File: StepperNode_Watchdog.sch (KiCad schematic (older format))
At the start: 5 parts

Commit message: First Revision -
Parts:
- removed R? (x2): 10K, symbol R
- removed U? (x2): TPS3813, symbol TPS3813
- removed U?: 74LVC1G32GW,125, symbol 74LVC1G32GW,125
- added R10, R9: 10K, RLOOP_FOOTPRINTS:rLoop_R_0603, symbol 10K
- added R5, R6, R7, R8: 0R, RLOOP_FOOTPRINTS:rLoop_R_0603, symbol 0R
- added U10, U11: TPS3813K33DBVT, RLOOP_FOOTPRINTS:rLoop_SOT236, symbol TPS3813K33DBVT
- added U12: 74LVC1G32GW,125, RLOOP_FOOTPRINTS:rLoop_SOT353, symbol 74LVC1G32GW,125
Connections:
- net labels added: +3V3_A, +3V3_B, GNDD
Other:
- note added: "DESIGN REVIEW NOTES:\n1. STEP_DIR_CTRL should go low if channel A fails, giving channel B priority\n2. STEP_DIR_CTRL is pulled up, so the only way it can go low is if the TPS3813 is powered\n3. All devices here need redundant supplies\n4. Need to provide isolation in case of parasitic power from a failed node."

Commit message: Update per design review.
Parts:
- added C? (x3): C_100nF_50V, RLOOP_FOOTPRINTS:rLoop_C_0603, symbol C_100nF_50V
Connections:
- net +3V3: now also C?.1, C?.1, C?.1
- net GNDD: now also C?.2, C?.2, C?.2
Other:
- note added: "Active High when either watchdog is good.\nThis signal then ensure the G210X enable circuits are kept closed except in\nthe case of a dual channel failure, where failsafe braking is required."
- note removed: "Active High when\nBoth watchdogs are good"
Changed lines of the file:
@@
 Title "Watchdog"
 Date ""
-Rev "1"
+Rev "2"
 Comp ""
 Comment1 ""
@@
 Text Label 9850 5150 0    60   ~ 0
 WDT_GOOD
-Text Notes 10000 5400 0    60   ~ 0
-Active High when\nBoth watchdogs are good
+Text Notes 10000 5600 0    60   ~ 0
+Active High when either watchdog is good.\nThis signal then ensure the G210X enable circuits are kept closed except in\nthe case of a dual channel failure, where failsafe braking is required.
 Text Notes 5750 6600 0    60   ~ 0
 Todo:\nJumper Pin to simulate failures.
@@
 	0    -1   -1   0
 $EndComp
+$Comp
+L C_100nF_50V C?
+U 1 1 575CF20D
+P 4150 4950
+F 0 "C?" H 4175 5050 50  0000 L CNN
+F 1 "C_100nF_50V" H 4175 4850 50  0000 L CNN
+F 2 "RLOOP_FOOTPRINTS:rLoop_C_0603" H 4188 4800 50  0001 C CNN
+F 3 "" H 4150 4950 50  0000 C CNN
+	1    4150 4950
+	1    0    0    -1
+$EndComp
+$Comp
+L +3V3_A #PWR?
+U 1 1 575CF256
+P 4150 4800
+F 0 "#PWR?" H 4150 4650 50  0001 C CNN
+F 1 "+3V3_A" H 4150 4940 50  0000 C CNN
+F 2 "" H 4150 4800 60  0000 C CNN
+F 3 "" H 4150 4800 60  0000 C CNN
+	1    4150 4800
+	1    0    0    -1
+$EndComp
+$Comp
+L GNDD #PWR?
+U 1 1 575CF268
+P 4150 5100
+F 0 "#PWR?" H 4150 4850 50  0001 C CNN
+F 1 "GNDD" H 4150 4950 50  0000 C CNN
+F 2 "" H 4150 5100 50  0000 C CNN
+F 3 "" H 4150 5100 50  0000 C CNN
+	1    4150 5100
+	1    0    0    -1
+$EndComp
+$Comp
+L C_100nF_50V C?
+U 1 1 575CF2F4
+P 4150 6050
+F 0 "C?" H 4175 6150 50  0000 L CNN
+F 1 "C_100nF_50V" H 4175 5950 50  0000 L CNN
+F 2 "RLOOP_FOOTPRINTS:rLoop_C_0603" H 4188 5900 50  0001 C CNN
+F 3 "" H 4150 6050 50  0000 C CNN
+	1    4150 6050
+	1    0    0    -1
+$EndComp
+$Comp
+L GNDD #PWR?
+U 1 1 575CF2FA
+P 4150 6200
+F 0 "#PWR?" H 4150 5950 50  0001 C CNN
+F 1 "GNDD" H 4150 6050 50  0000 C CNN
+F 2 "" H 4150 6200 50  0000 C CNN
+F 3 "" H 4150 6200 50  0000 C CNN
+	1    4150 6200
+	1    0    0    -1
+$EndComp
+$Comp
+L +3V3_B #PWR?
+U 1 1 575CF30D
+P 4150 5900
+F 0 "#PWR?" H 4150 5750 50  0001 C CNN
+F 1 "+3V3_B" H 4150 6040 50  0000 C CNN
+F 2 "" H 4150 5900 60  0000 C CNN
+F 3 "" H 4150 5900 60  0000 C CNN
+	1    4150 5900
+	1    0    0    -1
+$EndComp
+$Comp
+L C_100nF_50V C?
+U 1 1 575CF5E2
+P 9500 6200
+F 0 "C?" H 9525 6300 50  0000 L CNN
+F 1 "C_100nF_50V" H 9525 6100 50  0000 L CNN
+F 2 "RLOOP_FOOTPRINTS:rLoop_C_0603" H 9538 6050 50  0001 C CNN
+F 3 "" H 9500 6200 50  0000 C CNN
+	1    9500 6200
+	1    0    0    -1
+$EndComp
+$Comp
+L +3V3_A #PWR?
+U 1 1 575CF5E8
+P 9500 6050
+F 0 "#PWR?" H 9500 5900 50  0001 C CNN
+F 1 "+3V3_A" H 9500 6190 50  0000 C CNN
+F 2 "" H 9500 6050 60  0000 C CNN
+F 3 "" H 9500 6050 60  0000 C CNN
+	1    9500 6050
+	1    0    0    -1
+$EndComp
+$Comp
+L GNDD #PWR?
+U 1 1 575CF5EE
+P 9500 6350
+F 0 "#PWR?" H 9500 6100 50  0001 C CNN
+F 1 "GNDD" H 9500 6200 50  0000 C CNN
+F 2 "" H 9500 6350 50  0000 C CNN
+F 3 "" H 9500 6350 50  0000 C CNN
+	1    9500 6350
+	1    0    0    -1
+$EndComp
 $EndSCHEMATC

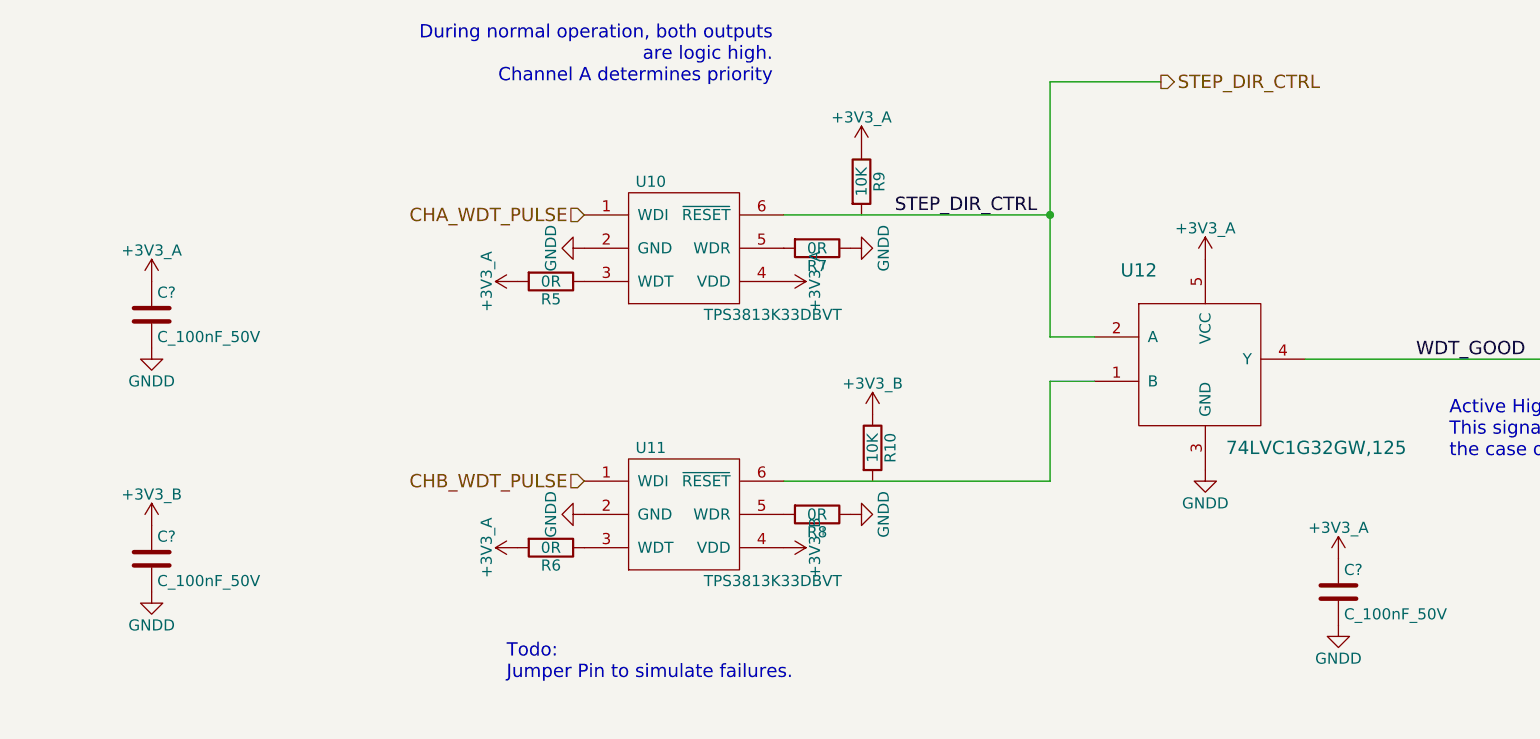
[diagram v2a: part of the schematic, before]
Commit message: Fix most ERC warnings (non-connected pins, etc)
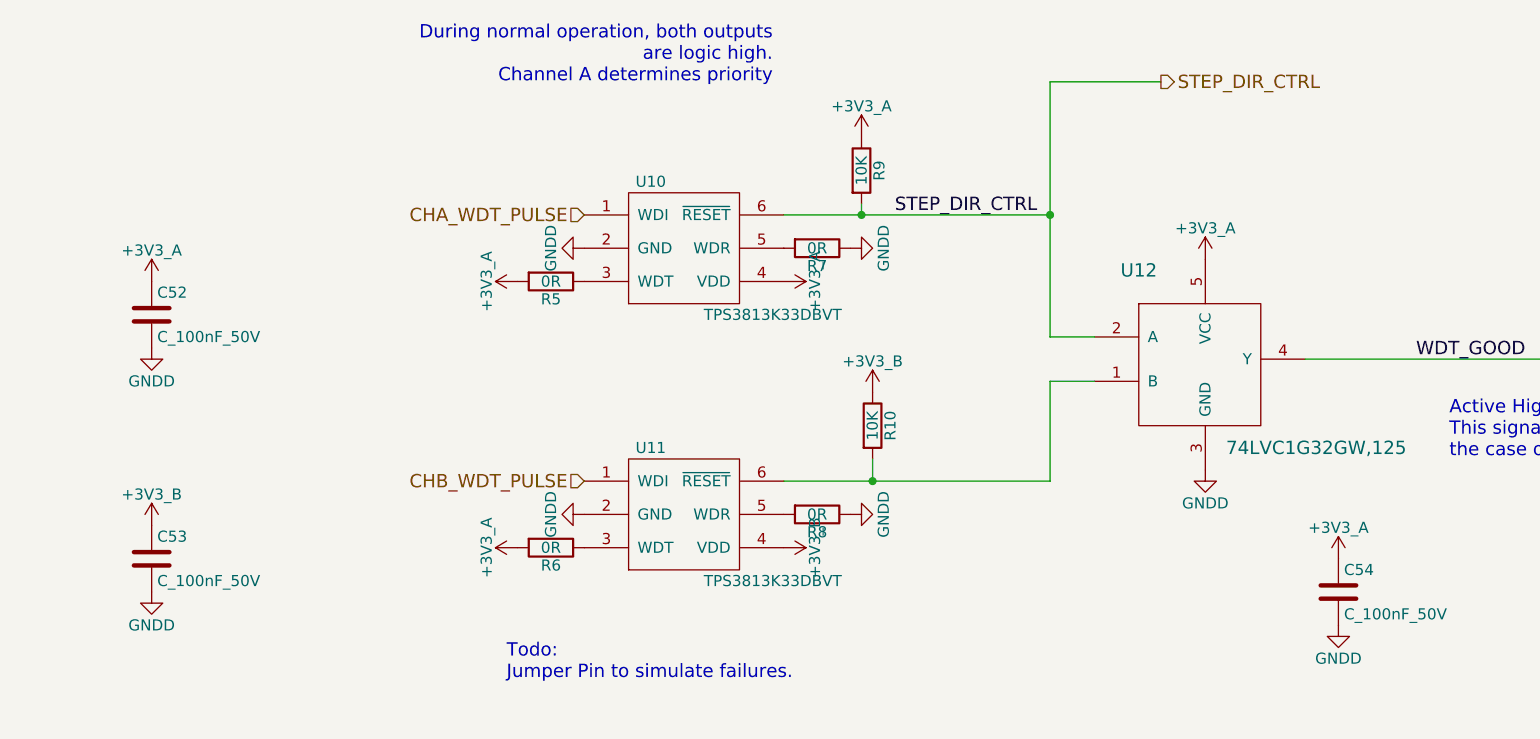
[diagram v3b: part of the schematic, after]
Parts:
- gave numbers to parts that had none: 3
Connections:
- net STEP_DIR_CTRL: now also R9.2
- net at R10.2: now also U11.6 (~RESET), U12.1 (B)
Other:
- moved on the sheet: R10, R9
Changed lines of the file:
@@
 L 10K R10
 U 1 1 575D4934
-P 7400 5550
-F 0 "R10" V 7480 5550 50  0000 C CNN
-F 1 "10K" V 7400 5550 50  0000 C CNN
-F 2 "RLOOP_FOOTPRINTS:rLoop_R_0603" V 7330 5550 50  0001 C CNN
-F 3 "" H 7400 5550 50  0000 C CNN
-	1    7400 5550
+P 7400 5450
+F 0 "R10" V 7480 5450 50  0000 C CNN
+F 1 "10K" V 7400 5450 50  0000 C CNN
+F 2 "RLOOP_FOOTPRINTS:rLoop_R_0603" V 7330 5450 50  0001 C CNN
+F 3 "" H 7400 5450 50  0000 C CNN
+	1    7400 5450
 	1    0    0    -1
 $EndComp
@@
 L 10K R9
 U 1 1 575D49D5
-P 7350 4350
-F 0 "R9" V 7430 4350 50  0000 C CNN
-F 1 "10K" V 7350 4350 50  0000 C CNN
-F 2 "RLOOP_FOOTPRINTS:rLoop_R_0603" V 7280 4350 50  0001 C CNN
-F 3 "" H 7350 4350 50  0000 C CNN
-	1    7350 4350
+P 7350 4300
+F 0 "R9" V 7430 4300 50  0000 C CNN
+F 1 "10K" V 7350 4300 50  0000 C CNN
+F 2 "RLOOP_FOOTPRINTS:rLoop_R_0603" V 7280 4300 50  0001 C CNN
+F 3 "" H 7350 4300 50  0000 C CNN
+	1    7350 4300
 	1    0    0    -1
 $EndComp
@@
 $EndComp
 $Comp
-L +3V3_A #PWR89
+L +3V3_A #PWR083
 U 1 1 5765507A
 P 8900 4700
-F 0 "#PWR89" H 8900 4550 50  0001 C CNN
+F 0 "#PWR083" H 8900 4550 50  0001 C CNN
 F 1 "+3V3_A" H 8900 4840 50  0000 C CNN
 F 2 "" H 8900 4700 60  0000 C CNN
@@
 $EndComp
 $Comp
-L GNDD #PWR90
+L GNDD #PWR084
 U 1 1 57655098
 P 8900 5650
-F 0 "#PWR90" H 8900 5400 50  0001 C CNN
+F 0 "#PWR084" H 8900 5400 50  0001 C CNN
 F 1 "GNDD" H 8900 5500 50  0000 C CNN
 F 2 "" H 8900 5650 50  0000 C CNN
@@
 $EndComp
 $Comp
-L GNDD #PWR81
+L GNDD #PWR085
 U 1 1 576552AD
 P 6100 4650
-F 0 "#PWR81" H 6100 4400 50  0001 C CNN
+F 0 "#PWR085" H 6100 4400 50  0001 C CNN
 F 1 "GNDD" H 6100 4500 50  0000 C CNN
 F 2 "" H 6100 4650 50  0000 C CNN
@@
 $EndComp
 $Comp
-L GNDD #PWR82
+L GNDD #PWR086
 U 1 1 57655309
 P 6100 5850
-F 0 "#PWR82" H 6100 5600 50  0001 C CNN
+F 0 "#PWR086" H 6100 5600 50  0001 C CNN
 F 1 "GNDD" H 6100 5700 50  0000 C CNN
 F 2 "" H 6100 5850 50  0000 C CNN
@@
 $EndComp
 $Comp
-L +3V3_A #PWR83
+L +3V3_A #PWR087
 U 1 1 576553D8
 P 7000 4800
-F 0 "#PWR83" H 7000 4650 50  0001 C CNN
+F 0 "#PWR087" H 7000 4650 50  0001 C CNN
 F 1 "+3V3_A" H 7000 4940 50  0000 C CNN
 F 2 "" H 7000 4800 60  0000 C CNN
@@
 $EndComp
 $Comp
-L +3V3_A #PWR87
+L +3V3_A #PWR088
 U 1 1 576553E5
-P 7350 4200
-F 0 "#PWR87" H 7350 4050 50  0001 C CNN
-F 1 "+3V3_A" H 7350 4340 50  0000 C CNN
-F 2 "" H 7350 4200 60  0000 C CNN
-F 3 "" H 7350 4200 60  0000 C CNN
-	1    7350 4200
+P 7350 4150
+F 0 "#PWR088" H 7350 4000 50  0001 C CNN
+F 1 "+3V3_A" H 7350 4290 50  0000 C CNN
+F 2 "" H 7350 4150 60  0000 C CNN
+F 3 "" H 7350 4150 60  0000 C CNN
+	1    7350 4150
 	1    0    0    -1
 $EndComp
@@
 	7000 5700 8200 5700
 $Comp
-L +3V3_B #PWR84
+L +3V3_B #PWR089
 U 1 1 576560EA
 P 7000 6000
-F 0 "#PWR84" H 7000 5850 50  0001 C CNN
+F 0 "#PWR089" H 7000 5850 50  0001 C CNN
 F 1 "+3V3_B" H 7000 6140 50  0000 C CNN
 F 2 "" H 7000 6000 60  0000 C CNN
@@
 $EndComp
 $Comp
-L +3V3_B #PWR88
+L +3V3_B #PWR090
 U 1 1 5765612F
-P 7400 5400
-F 0 "#PWR88" H 7400 5250 50  0001 C CNN
-F 1 "+3V3_B" H 7400 5540 50  0000 C CNN
-F 2 "" H 7400 5400 60  0000 C CNN
-F 3 "" H 7400 5400 60  0000 C CNN
-	1    7400 5400
+P 7400 5300
+F 0 "#PWR090" H 7400 5150 50  0001 C CNN
+F 1 "+3V3_B" H 7400 5440 50  0000 C CNN
+F 2 "" H 7400 5300 60  0000 C CNN
+F 3 "" H 7400 5300 60  0000 C CNN
+	1    7400 5300
 	1    0    0    -1
 $EndComp
@@
 $EndComp
 $Comp
-L GNDD #PWR86
+L GNDD #PWR091
 U 1 1 57656D26
 P 7300 5850
-F 0 "#PWR86" H 7300 5600 50  0001 C CNN
+F 0 "#PWR091" H 7300 5600 50  0001 C CNN
 F 1 "GNDD" H 7300 5700 50  0000 C CNN
 F 2 "" H 7300 5850 50  0000 C CNN
@@
 $EndComp
 $Comp
-L GNDD #PWR85
+L GNDD #PWR092
 U 1 1 57656DA2
 P 7300 4650
-F 0 "#PWR85" H 7300 4400 50  0001 C CNN
+F 0 "#PWR092" H 7300 4400 50  0001 C CNN
 F 1 "GNDD" H 7300 4500 50  0000 C CNN
 F 2 "" H 7300 4650 50  0000 C CNN
@@
 $EndComp
 $Comp
-L +3V3_A #PWR79
+L +3V3_A #PWR093
 U 1 1 57656DB3
 P 5800 4800
-F 0 "#PWR79" H 5800 4650 50  0001 C CNN
+F 0 "#PWR093" H 5800 4650 50  0001 C CNN
 F 1 "+3V3_A" H 5800 4940 50  0000 C CNN
 F 2 "" H 5800 4800 60  0000 C CNN
@@
 $EndComp
 $Comp
-L +3V3_A #PWR80
+L +3V3_A #PWR094
 U 1 1 57656E70
 P 5800 6000
-F 0 "#PWR80" H 5800 5850 50  0001 C CNN
+F 0 "#PWR094" H 5800 5850 50  0001 C CNN
 F 1 "+3V3_A" H 5800 6140 50  0000 C CNN
 F 2 "" H 5800 6000 60  0000 C CNN
@@
 $EndComp
 $Comp
-L C_100nF_50V C?
+L C_100nF_50V C52
 U 1 1 575CF20D
 P 4150 4950
-F 0 "C?" H 4175 5050 50  0000 L CNN
+F 0 "C52" H 4175 5050 50  0000 L CNN
 F 1 "C_100nF_50V" H 4175 4850 50  0000 L CNN
 F 2 "RLOOP_FOOTPRINTS:rLoop_C_0603" H 4188 4800 50  0001 C CNN
@@
 $EndComp
 $Comp
-L +3V3_A #PWR?
+L +3V3_A #PWR095
 U 1 1 575CF256
 P 4150 4800
-F 0 "#PWR?" H 4150 4650 50  0001 C CNN
+F 0 "#PWR095" H 4150 4650 50  0001 C CNN
 F 1 "+3V3_A" H 4150 4940 50  0000 C CNN
 F 2 "" H 4150 4800 60  0000 C CNN
@@
 $EndComp
 $Comp
-L GNDD #PWR?
+L GNDD #PWR096
 U 1 1 575CF268
 P 4150 5100
-F 0 "#PWR?" H 4150 4850 50  0001 C CNN
+F 0 "#PWR096" H 4150 4850 50  0001 C CNN
 F 1 "GNDD" H 4150 4950 50  0000 C CNN
 F 2 "" H 4150 5100 50  0000 C CNN
@@
 $EndComp
 $Comp
-L C_100nF_50V C?
+L C_100nF_50V C53
 U 1 1 575CF2F4
 P 4150 6050
-F 0 "C?" H 4175 6150 50  0000 L CNN
+F 0 "C53" H 4175 6150 50  0000 L CNN
 F 1 "C_100nF_50V" H 4175 5950 50  0000 L CNN
 F 2 "RLOOP_FOOTPRINTS:rLoop_C_0603" H 4188 5900 50  0001 C CNN
@@
 $EndComp
 $Comp
-L GNDD #PWR?
+L GNDD #PWR097
 U 1 1 575CF2FA
 P 4150 6200
-F 0 "#PWR?" H 4150 5950 50  0001 C CNN
+F 0 "#PWR097" H 4150 5950 50  0001 C CNN
 F 1 "GNDD" H 4150 6050 50  0000 C CNN
 F 2 "" H 4150 6200 50  0000 C CNN
@@
 $EndComp
 $Comp
-L +3V3_B #PWR?
+L +3V3_B #PWR098
 U 1 1 575CF30D
 P 4150 5900
-F 0 "#PWR?" H 4150 5750 50  0001 C CNN
+F 0 "#PWR098" H 4150 5750 50  0001 C CNN
 F 1 "+3V3_B" H 4150 6040 50  0000 C CNN
 F 2 "" H 4150 5900 60  0000 C CNN
@@
 $EndComp
 $Comp
-L C_100nF_50V C?
+L C_100nF_50V C54
 U 1 1 575CF5E2
 P 9500 6200
-F 0 "C?" H 9525 6300 50  0000 L CNN
+F 0 "C54" H 9525 6300 50  0000 L CNN
 F 1 "C_100nF_50V" H 9525 6100 50  0000 L CNN
 F 2 "RLOOP_FOOTPRINTS:rLoop_C_0603" H 9538 6050 50  0001 C CNN
@@
 $EndComp
 $Comp
-L +3V3_A #PWR?
+L +3V3_A #PWR099
 U 1 1 575CF5E8
 P 9500 6050
-F 0 "#PWR?" H 9500 5900 50  0001 C CNN
+F 0 "#PWR099" H 9500 5900 50  0001 C CNN
 F 1 "+3V3_A" H 9500 6190 50  0000 C CNN
 F 2 "" H 9500 6050 60  0000 C CNN
@@
 $EndComp
 $Comp
-L GNDD #PWR?
+L GNDD #PWR0100
 U 1 1 575CF5EE
 P 9500 6350
-F 0 "#PWR?" H 9500 6100 50  0001 C CNN
+F 0 "#PWR0100" H 9500 6100 50  0001 C CNN
 F 1 "GNDD" H 9500 6200 50  0000 C CNN
 F 2 "" H 9500 6350 50  0000 C CNN
@@
 	1    0    0    -1
 $EndComp
+Wire Wire Line
+	7350 4450 7350 4500
+Connection ~ 7350 4500
+Wire Wire Line
+	7400 5600 7400 5700
+Connection ~ 7400 5700
 $EndSCHEMATC
